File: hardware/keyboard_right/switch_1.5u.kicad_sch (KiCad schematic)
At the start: 4 parts

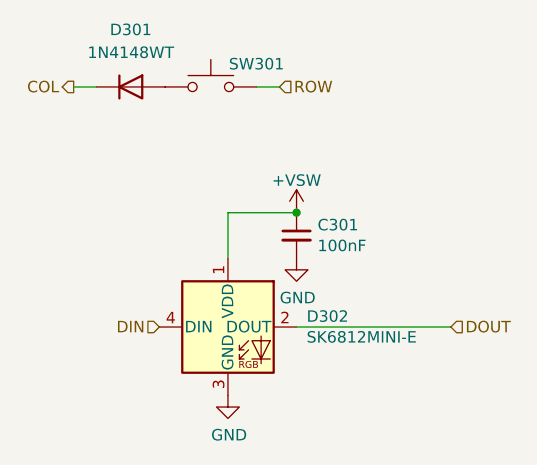
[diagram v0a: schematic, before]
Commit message: Update after producion of rev 2
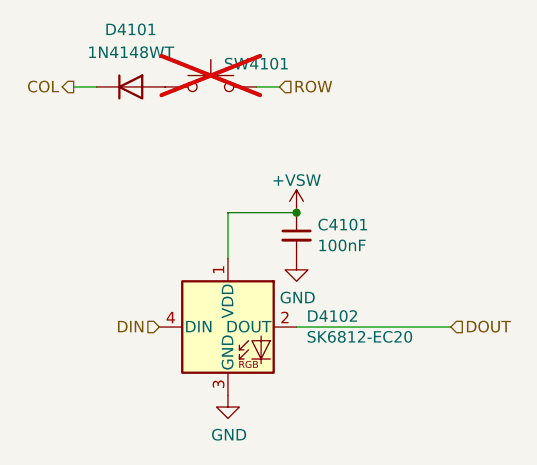
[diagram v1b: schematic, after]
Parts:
- C4101: renamed from C301; footprint Capacitor_SMD:C_0603_1608Metric_Pad1.08x0.95mm_HandSolder -> Capacitor_SMD:C_0402_1005Metric; LCSC (none) -> C1525
- D4101: renamed from D301; LCSC (none) -> C27748
- D4102: renamed from D302; value SK6812MINI-E -> SK6812-EC20; footprint prettylib:SK6812MINI-E-reversible -> prettylib:sk6812-ec20; LCSC (none) -> C2909058; Product name SK6812MINI-E -> SK6812-EC20
- SW4101: renamed from SW301; now not fitted
